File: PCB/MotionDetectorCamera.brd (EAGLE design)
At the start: 41.9 x 32.6 mm, 185 parts, among them J1 JUMPER-SOLDER, J10 MICROSD-SOCKET, J11 USB-C-JACK, J2 JUMPER-SOLDER, J3 JUMPER-SOLDER, J4 JUMPER-SOLDER, J5 JST-SM02B-SRSS-TB, J6 JUMPER-SOLDER, J7 JUMPER-SOLDER, J8 JUMPER-SOLDER, J9 S-MOUNT-LENS-HOLDERM12LENSES-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, Q1 PMOS-NEXPERIA-SOT1220, Q2 PMOS-NEXPERIA-SOT1220, Q3 PMOS-NEXPERIA-SOT1220, U1 TI-TPS2116, U10 TI-TPS22919DCK, U11 TI-TPS62A01, U13 TI-TPS22919DCK, U14 TI-TPS22919DCK, U15 TI-MSP430FR2422IRHL, U16 NXP-NTB0102, U17 NXP-NTB0102, U18 PANASONIC-EKMB110711X, U19 LATTICE-ICE40HX4K-BG121, U2 DIODESINC-AP7350, U20 WINBOND-W25Q40EW, U21 NEXPERIA-74LVC1G98-OR-INV-INP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, U22 NEXPERIA-74LVC1G98-BUFFER, U23 ON-AR0330CS1C12SPKA0, U24 ALLIANCE-AS4C8M16MSA-6BIN, U25 STM-STM32F730, U26 DIODESINC-DT1446-04V-7, U27 NEXPERIA-74LVC1G98-BUFFER, U3 NEXPERIA-74LVC1G98-NOR, U4 MICROCHIP-MCP7383X, U5 EATON-STN101, U6 TI-TPS62A01, U7 TI-TPS62A01, U9 TI-TPS22919DCK, X1 EPSON-FC-135, X2 SITIME-SIT8021, X3 SITIME-SIT8021

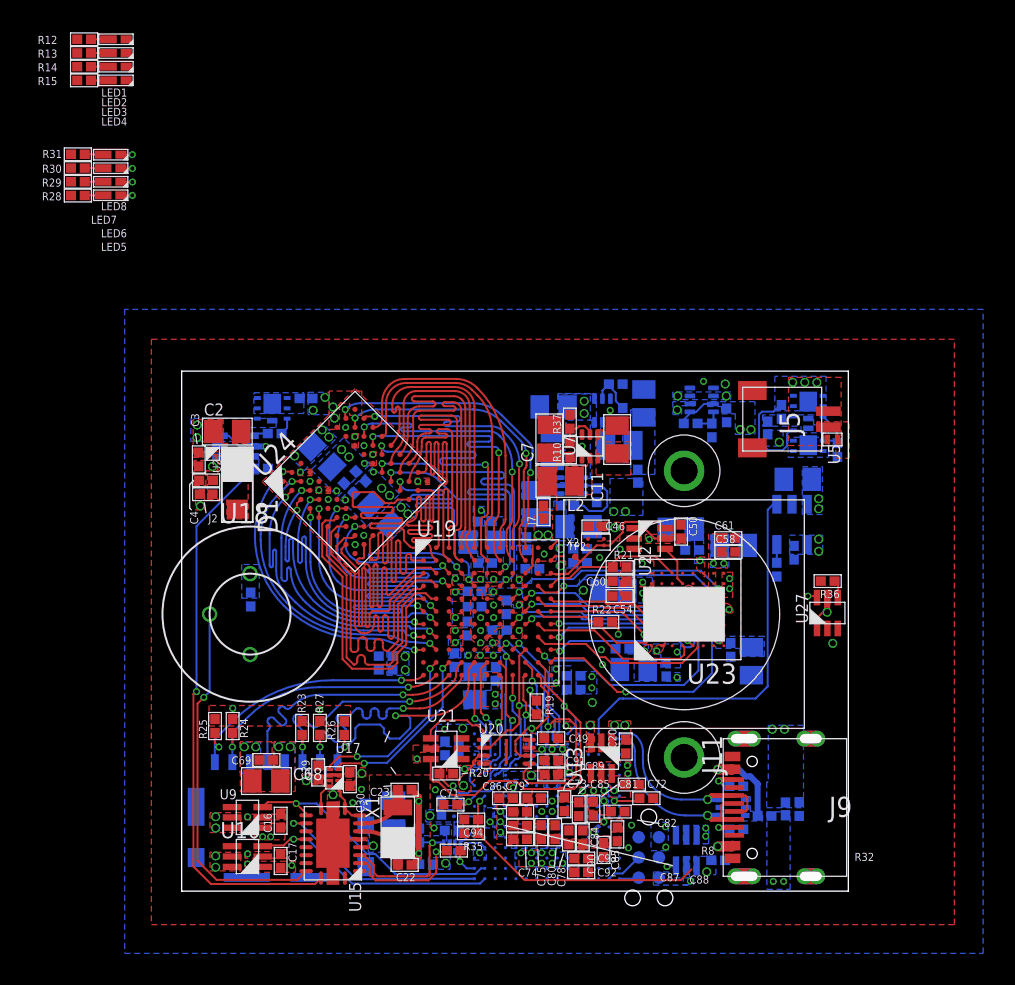
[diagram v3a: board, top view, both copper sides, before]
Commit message: 32 airwires
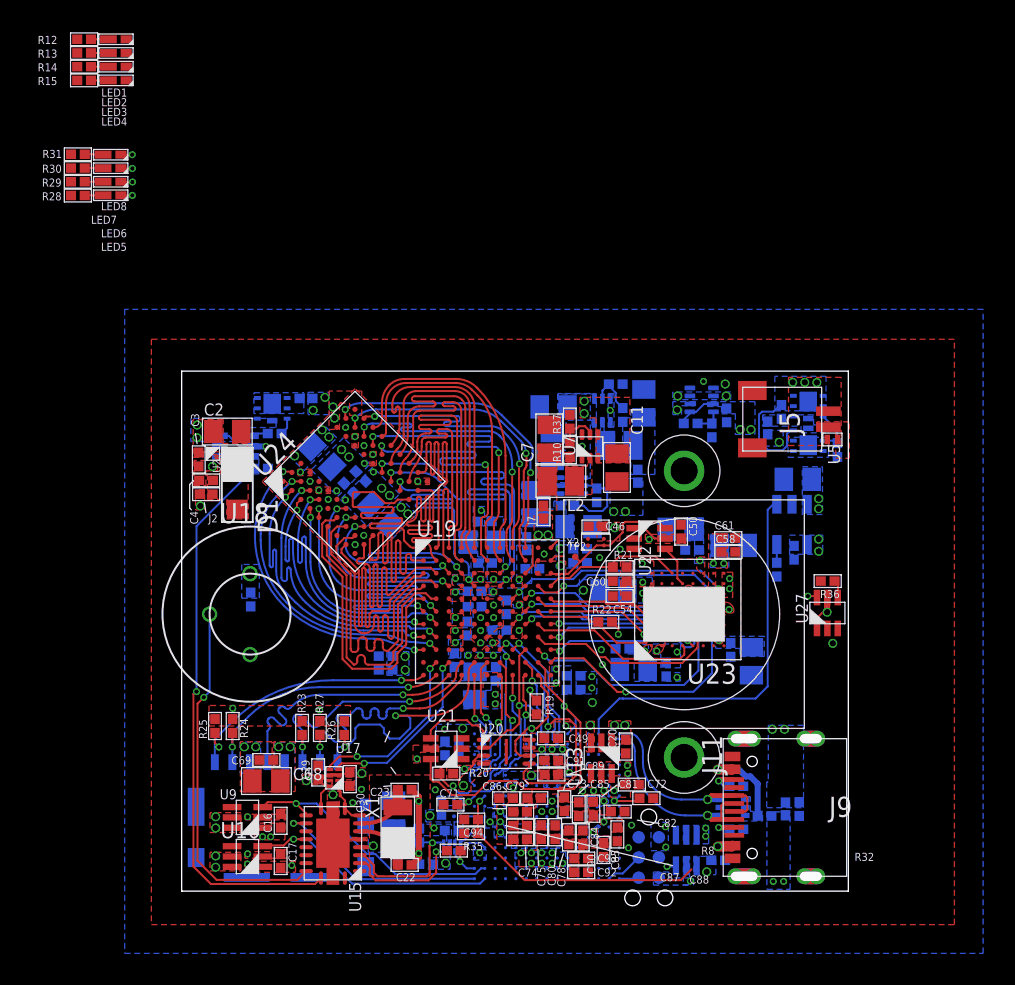
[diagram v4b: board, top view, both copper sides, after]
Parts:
- moved C11 1.76 mm to (27.3, 26.6), turned to 270 degrees
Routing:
- net VDD_A_3V3: track 72.0 -> 72.6 mm

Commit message: 30 airwires
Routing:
- net VDD_B_1V8_STM: track 44.3 -> 49.9 mm
- net GND: vias 57 -> 58
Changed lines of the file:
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@@
 </polygon>
 <via x="11.30808125" y="7.3914" extent="1-16" drill="0.381"/>
-<wire x1="18.94658125" y1="8.506165625" x2="21.81578125" y2="9.006165625" width="0" layer="19" extent="1-1"/>
 </signal>
 <signal name="GND">
@@
 <vertex x="27.142440625" y="31.242"/>
 </polygon>
+<via x="7.74191875" y="6.0706" extent="1-16" drill="0.254"/>
 <wire x1="30.7972" y1="18.657" x2="30.7972" y2="18.007" width="0" layer="19" extent="1-1"/>
 <wire x1="30.7972" y1="17.357" x2="30.7972" y2="18.007" width="0" layer="19" extent="1-1"/>
@@
 <wire x1="34.47018125" y1="14.71458125" x2="33.3972" y2="15.407" width="0" layer="19" extent="1-16"/>
 <wire x1="26.052784375" y1="24.416325" x2="25.7902625" y2="22.882859375" width="0" layer="19" extent="16-16"/>
-<wire x1="8.56711875" y1="7.88614375" x2="9.849459375" y2="6.940978125" width="0" layer="19" extent="1-1"/>
 <wire x1="35.2525625" y1="6.584259375" x2="34.576759375" y2="8.45348125" width="0" layer="19" extent="1-16"/>
 <wire x1="33.78918125" y1="5.25348125" x2="35.2525625" y2="6.584259375" width="0" layer="19" extent="16-16"/>
@@
 <wire x1="30.2665375" y1="1.7527" x2="30.472378125" y2="1.546859375" width="0.635" layer="15"/>
 <wire x1="23.905765625" y1="1.7527" x2="30.2665375" y2="1.7527" width="0.635" layer="15"/>
-<wire x1="20.817121875" y1="6.4923375" x2="17.650465625" y2="9.65899375" width="0.635" layer="15"/>
-<wire x1="17.650465625" y1="9.65899375" x2="17.650465625" y2="10.222021875" width="0.635" layer="15"/>
 <wire x1="18.707240625" y1="2.4069" x2="18.707803125" y2="2.4069" width="0.508" layer="15"/>
 <wire x1="23.25298125" y1="8.902803125" x2="23.259878125" y2="8.9097" width="0.508" layer="15"/>
 <wire x1="23.259878125" y1="8.9097" x2="23.905403125" y2="8.9097" width="0.508" layer="15"/>
+<wire x1="15.5854375" y1="4.73561875" x2="15.3464375" y2="4.97461875" width="0.635" layer="15"/>
+<wire x1="15.3464375" y1="4.97461875" x2="14.610525" y2="4.97461875" width="0.635" layer="15"/>
+<wire x1="14.610525" y1="4.97461875" x2="13.97" y2="5.61514375" width="0.635" layer="15"/>
+<wire x1="13.97" y1="9.27228125" x2="16.064859375" y2="11.367140625" width="0.635" layer="15"/>
+<wire x1="13.97" y1="5.61514375" x2="13.97" y2="9.27228125" width="0.635" layer="15"/>
+<wire x1="16.064859375" y1="11.367140625" x2="16.505346875" y2="11.367140625" width="0.635" layer="15"/>
+<wire x1="16.505346875" y1="11.367140625" x2="17.650465625" y2="10.222021875" width="0.635" layer="15"/>
 </signal>
 <signal name="VDD_B_1V8_IMG_SD">
@@
 <vertex x="5.7785" y="9.3762"/>
 <vertex x="5.7785" y="6.252"/>
-<vertex x="7.127240625" y="6.252"/>
-<vertex x="7.127240625" y="9.3762"/>
+<vertex x="6.731" y="6.252"/>
+<vertex x="6.731" y="8.7249"/>
+<vertex x="7.045959375" y="8.7249"/>
+<vertex x="7.045959375" y="9.3762"/>
 </polygon>
 <wire x1="6.090928125" y1="9.057684375" x2="6.80935" y2="9.057684375" width="0.635" layer="15"/>

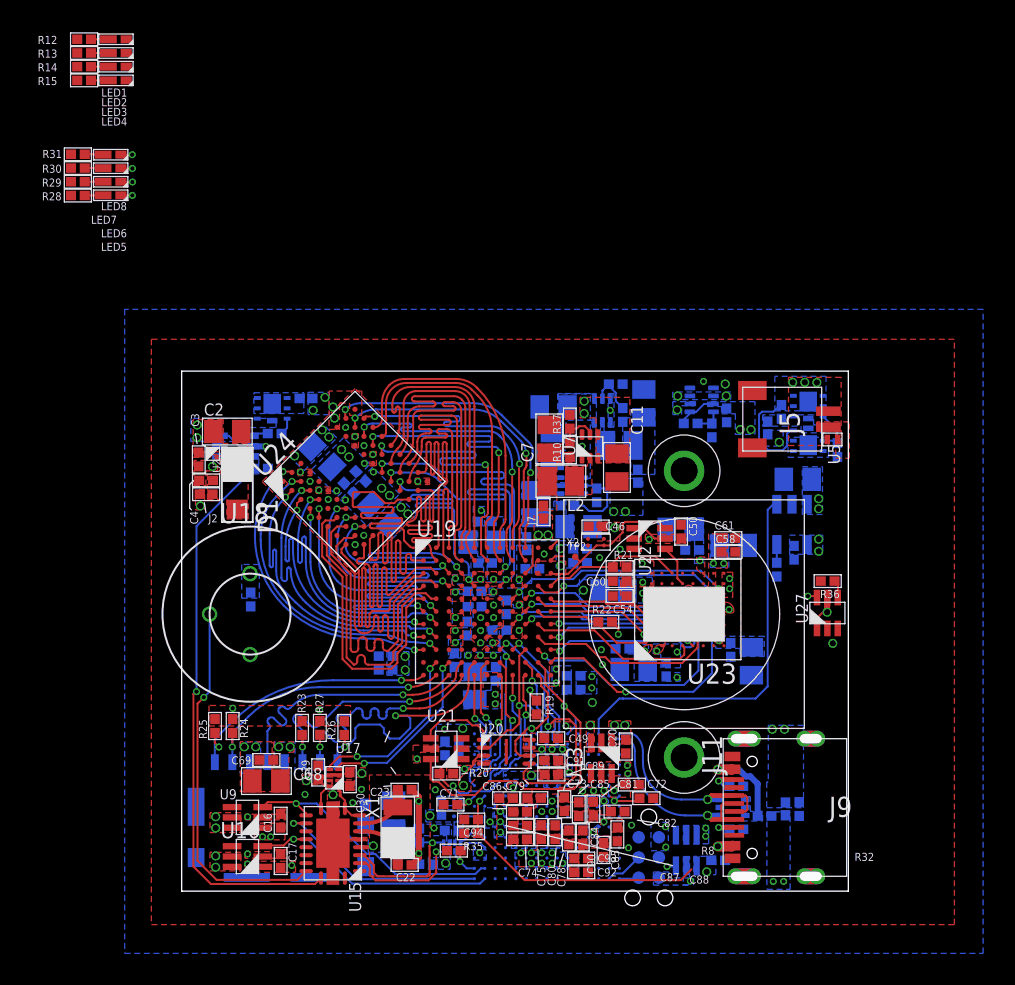
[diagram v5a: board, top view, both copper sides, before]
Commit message: Laid out ICE40 leds; 22 airwires to go
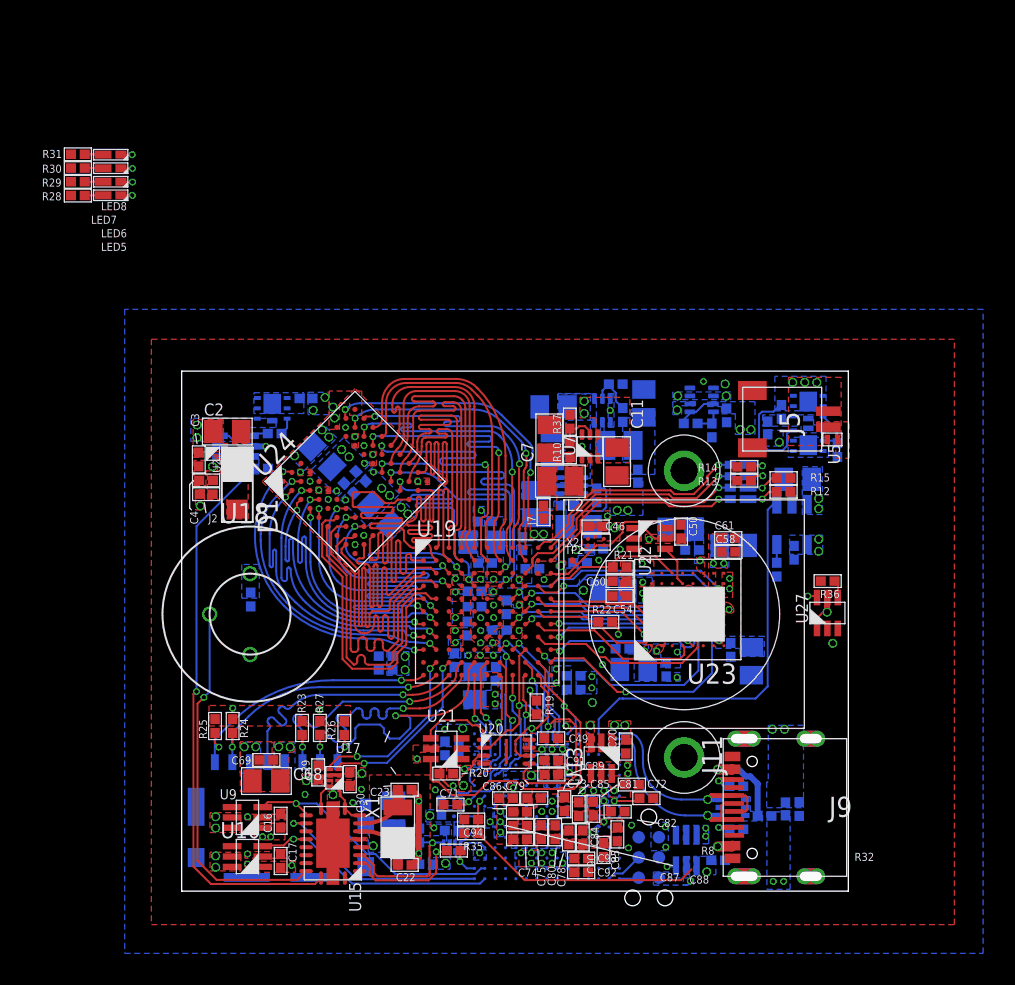
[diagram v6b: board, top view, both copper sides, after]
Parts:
- moved R12 52.3 mm to (37.8, 25.1), turned to 0 degrees
- moved R15 50.5 mm to (37.8, 25.9), turned to 0 degrees
- moved R13 49.4 mm to (35.3, 25.8)
- moved LED1 48.7 mm to (35.1, 24.6), flipped to the bottom
- moved R14 48.5 mm to (35.3, 26.6)
- moved LED2 47.4 mm to (35.1, 26.0), flipped to the bottom
- moved LED4 46.8 mm to (35.1, 25.3), flipped to the bottom
- moved LED3 46.5 mm to (35.1, 26.8), flipped to the bottom
- moved C42 1.02 mm to (26.0, 21.5)
- moved C11 0.38 mm to (27.3, 27.0)
- moved TP2 0.29 mm to (24.5, 20.8)
- moved J6 0.25 mm to (21.4, 21.8)
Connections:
- net ICE_LED0: now also LED3.A, U19.A10; no longer LED4.A, U19.C9
- net ICE_LED1: now also LED2.A, U19.A11; no longer LED3.A, U19.A10
- net ICE_LED2: now also LED4.A, U19.C9; no longer LED2.A, U19.A11
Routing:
- net ICE_LED2: track 0.68 -> 16.0 mm, vias 0 -> 1
- net ICE_LED1: track 0.00 -> 13.6 mm, vias 0 -> 1
- net ICE_LED0: track 1.93 -> 14.9 mm, vias 0 -> 1
- net ICE_LED3: track 0.91 -> 13.5 mm, vias 0 -> 1
- net N$23: track 1.10 -> 2.07 mm, vias 0 -> 1
- net N$28: track 1.10 -> 1.99 mm, vias 0 -> 1
- net N$26: track 1.10 -> 1.79 mm, vias 0 -> 1
- net N$20: track 1.10 -> 1.67 mm, vias 0 -> 1
- net GND: vias 58 -> 59

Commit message: Laid out leds
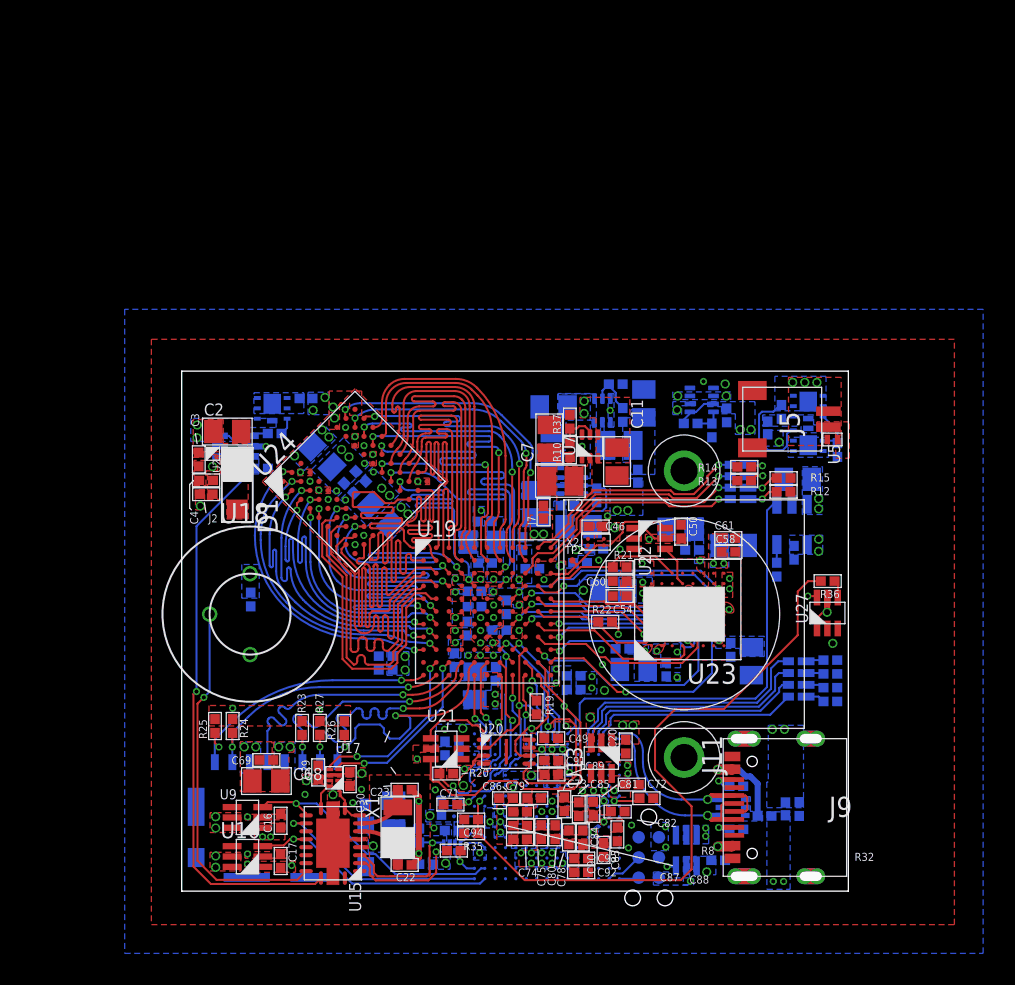
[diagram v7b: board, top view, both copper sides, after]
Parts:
- moved R28 56.9 mm to (40.7, 11.9), flipped to the bottom
- moved R29 56.9 mm to (40.7, 12.8), flipped to the bottom
- moved R30 56.9 mm to (40.7, 13.6), flipped to the bottom
- moved R31 56.9 mm to (40.7, 14.5), flipped to the bottom
- moved LED8 53.6 mm to (38.7, 14.4), flipped to the bottom
- moved LED7 53.6 mm to (38.7, 13.7), flipped to the bottom
- moved LED6 53.5 mm to (38.7, 13.0), flipped to the bottom
- moved LED5 53.4 mm to (38.7, 12.2), flipped to the bottom
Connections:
- net BAT_CHRG_STAT: now also U25.R11; no longer U25.R13
- net STM_LED0: now also U25.R12
- net STM_LED1: now also U25.P12
- net STM_LED2: now also U25.R13
- net STM_LED3: now also U25.P13
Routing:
- net BAT_CHRG_LVL: track 17.4 -> 43.0 mm
- net STM_LED0: track 0.71 -> 15.7 mm, vias 1 -> 0
- net STM_LED1: track 0.73 -> 15.6 mm, vias 1 -> 0
- net STM_LED2: track 0.73 -> 13.8 mm, vias 1 -> 0
- net STM_LED3: track 0.72 -> 13.7 mm, vias 1 -> 0
- net BAT_CHRG_STAT: track 24.2 -> 26.0 mm
